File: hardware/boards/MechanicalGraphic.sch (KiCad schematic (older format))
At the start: 1 part

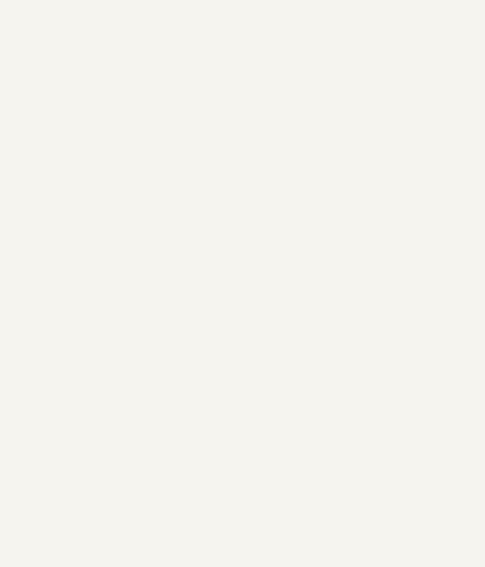
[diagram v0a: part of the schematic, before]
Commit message: In an AHDH fuled stupor I made a bunch of changes, only the last of which I recall, which would be adding fiducials
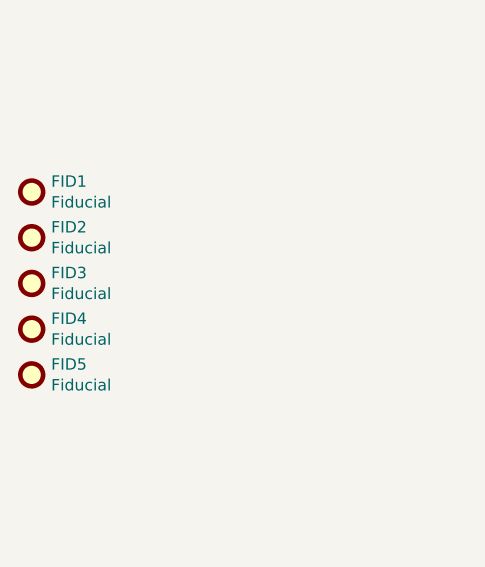
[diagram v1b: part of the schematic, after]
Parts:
- added FID1, FID2, FID3, FID4, FID5: Fiducial, Fiducial:Fiducial_0.5mm_Mask1mm, symbol Mechanical:Fiducial
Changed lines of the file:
@@
+	1    0    0    -1
+$EndComp
+$Comp
+L Mechanical:Fiducial FID1
+U 1 1 5F8348AA
+P 1600 1750
+F 0 "FID1" H 1685 1796 50  0000 L CNN
+F 1 "Fiducial" H 1685 1705 50  0000 L CNN
+F 2 "Fiducial:Fiducial_0.5mm_Mask1mm" H 1600 1750 50  0001 C CNN
+F 3 "~" H 1600 1750 50  0001 C CNN
+	1    1600 1750
+	1    0    0    -1
+$EndComp
+$Comp
+L Mechanical:Fiducial FID2
+U 1 1 5F834CBD
+P 1600 1950
+F 0 "FID2" H 1685 1996 50  0000 L CNN
+F 1 "Fiducial" H 1685 1905 50  0000 L CNN
+F 2 "Fiducial:Fiducial_0.5mm_Mask1mm" H 1600 1950 50  0001 C CNN
+F 3 "~" H 1600 1950 50  0001 C CNN
+	1    1600 1950
+	1    0    0    -1
+$EndComp
+$Comp
+L Mechanical:Fiducial FID3
+U 1 1 5F834E9D
+P 1600 2150
+F 0 "FID3" H 1685 2196 50  0000 L CNN
+F 1 "Fiducial" H 1685 2105 50  0000 L CNN
+F 2 "Fiducial:Fiducial_0.5mm_Mask1mm" H 1600 2150 50  0001 C CNN
+F 3 "~" H 1600 2150 50  0001 C CNN
+	1    1600 2150
+	1    0    0    -1
+$EndComp
+$Comp
+L Mechanical:Fiducial FID4
+U 1 1 5F8350D3
+P 1600 2350
+F 0 "FID4" H 1685 2396 50  0000 L CNN
+F 1 "Fiducial" H 1685 2305 50  0000 L CNN
+F 2 "Fiducial:Fiducial_0.5mm_Mask1mm" H 1600 2350 50  0001 C CNN
+F 3 "~" H 1600 2350 50  0001 C CNN
+	1    1600 2350
+	1    0    0    -1
+$EndComp
+$Comp
+L Mechanical:Fiducial FID5
+U 1 1 5F83529D
+P 1600 2550
+F 0 "FID5" H 1685 2596 50  0000 L CNN
+F 1 "Fiducial" H 1685 2505 50  0000 L CNN
+F 2 "Fiducial:Fiducial_0.5mm_Mask1mm" H 1600 2550 50  0001 C CNN
+F 3 "~" H 1600 2550 50  0001 C CNN
+	1    1600 2550
 	1    0    0    -1
 $EndComp

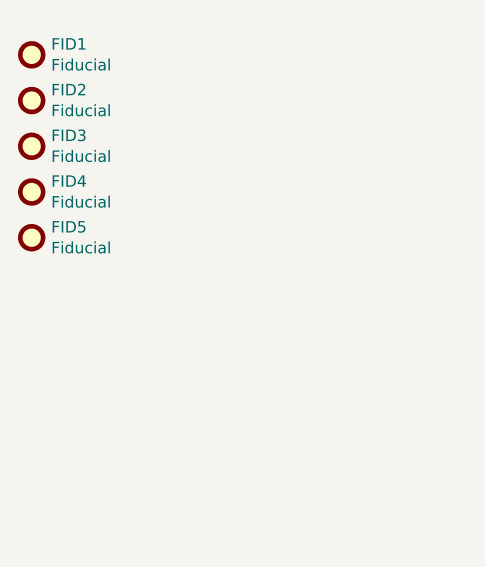
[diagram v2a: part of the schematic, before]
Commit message: Updated the PCB with the new parts for PHY reset logic and added another fiducial for the other SPI flash
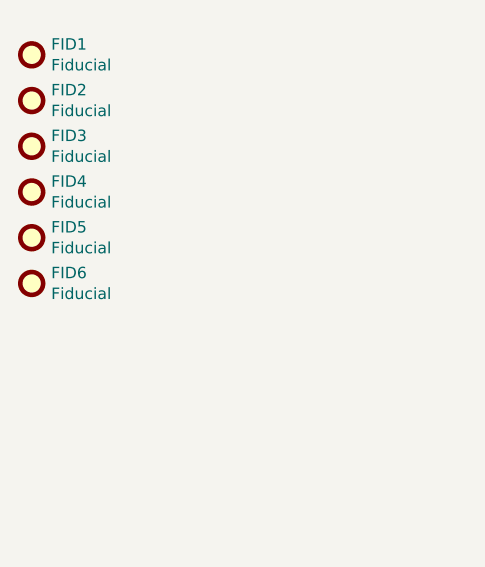
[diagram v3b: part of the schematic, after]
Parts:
- added FID6: Fiducial, Fiducial:Fiducial_0.5mm_Mask1mm, symbol Mechanical:Fiducial
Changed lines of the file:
@@
 $Descr A3 16535 11693
 encoding utf-8
-Sheet 5 11
+Sheet 4 11
 Title "lethallink - Mechanical and Graphics"
 Date "2020-06-14"
@@
 	1    0    0    -1
 $EndComp
+$Comp
+L Mechanical:Fiducial FID6
+U 1 1 60C6DEAE
+P 1600 2750
+F 0 "FID6" H 1685 2796 50  0000 L CNN
+F 1 "Fiducial" H 1685 2705 50  0000 L CNN
+F 2 "Fiducial:Fiducial_0.5mm_Mask1mm" H 1600 2750 50  0001 C CNN
+F 3 "~" H 1600 2750 50  0001 C CNN
+	1    1600 2750
+	1    0    0    -1
+$EndComp
